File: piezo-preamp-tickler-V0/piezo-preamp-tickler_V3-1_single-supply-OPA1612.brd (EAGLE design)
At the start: 100 x 66 mm, 54 parts, among them IC1 OPA1612, J2 phone/mixer-switch, J3 phone/mixer-switch, Q1 J201, Q1A 2N5486, Q2 MMBFJ201, Q2A 2N5486

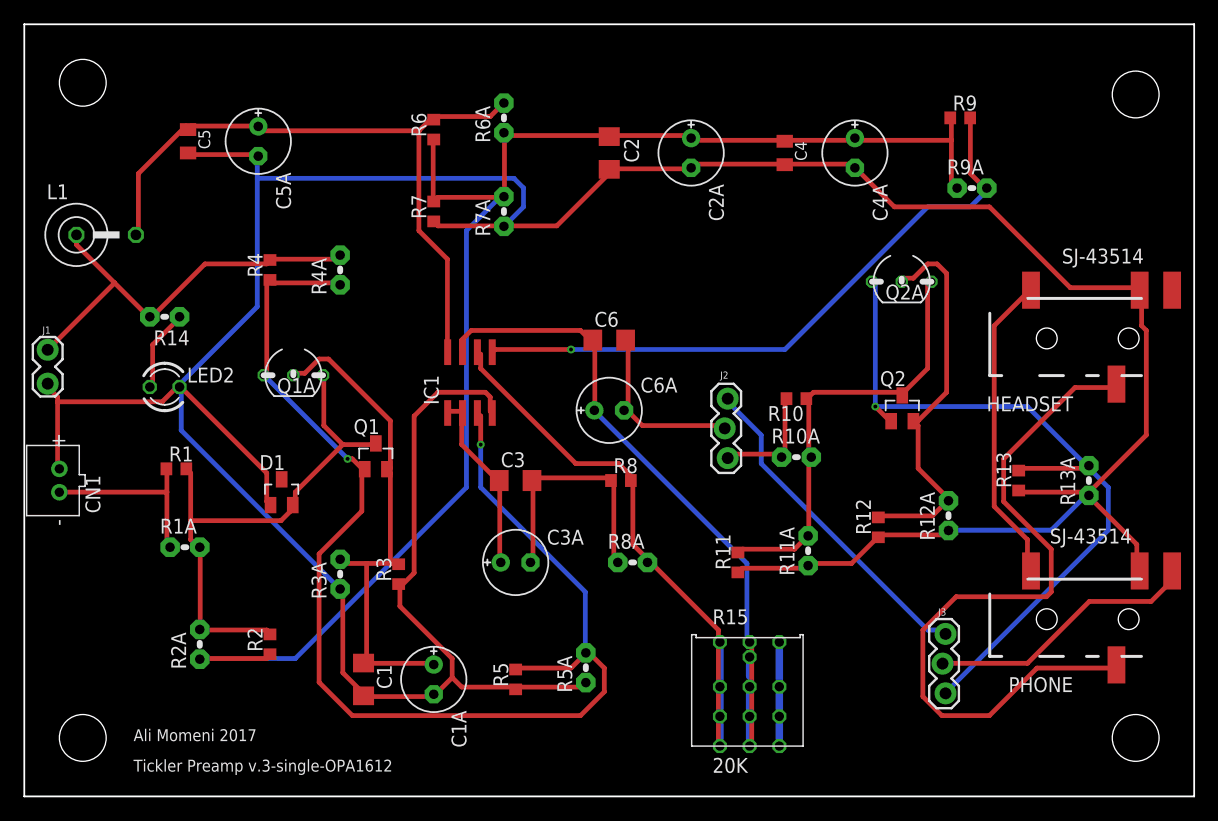
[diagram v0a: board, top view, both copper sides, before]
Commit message: new version so of piezo pickups
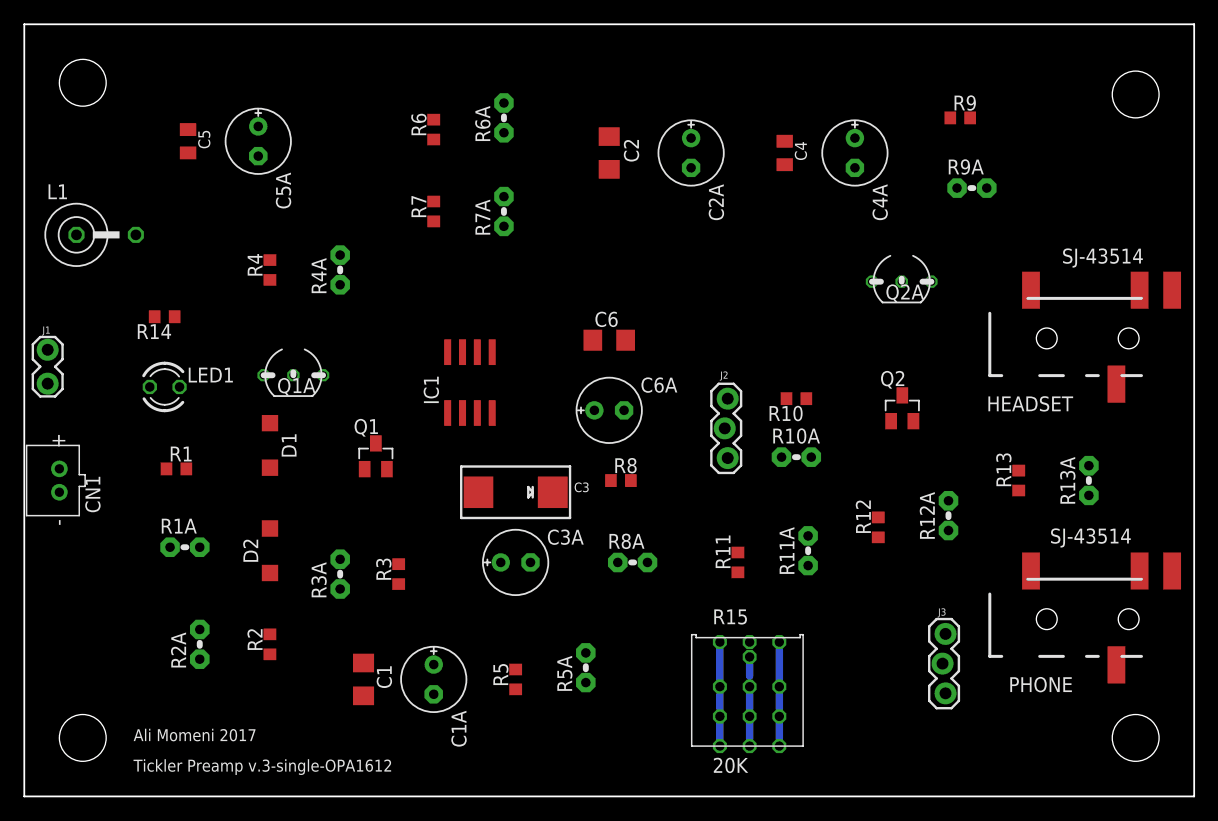
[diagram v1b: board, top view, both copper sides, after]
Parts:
- added D2: 1N4148W, CMU-ArtFab:SOD123
- C3: value 100uF -> mnove; device adafruit:C1206 -> microbuilder:EIA7343-31/D-R
- C4A: value 10uF -> 0.1uF
- D1: value BAT54S -> 1N4148W; device diode:SOT23 -> CMU-ArtFab:SOD123
- R14: device CMU-ArtFab:0204V -> CMU-ArtFab:R0603
- moved D1 4.12 mm to (21.0, 30.0), turned to 270 degrees
- moved C3 1.00 mm to (42.0, 26.0)
- renumbered LED2 to LED1
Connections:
- new net N$4: D1.A, D2.A
- net GATE1: now also D1.C; no longer D1.2
- net GND: now also D2.C; no longer D1.1
- net N$1: now also C3.+; no longer C3.1
- net N$52: now also C3.-; no longer C3.2
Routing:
- net GND: track 309.5 -> 0.00 mm
- net N$35: track 123.3 -> 0.00 mm
- net DRAINE1: track 107.8 -> 0.00 mm, vias 2 -> 0
- net NAME: track 65.1 -> 0.00 mm, vias 1 -> 0
- net N$45: track 62.4 -> 0.00 mm
- net N$32: track 59.9 -> 0.00 mm
- net N$16: track 54.8 -> 0.00 mm, vias 1 -> 0
- net N$31: track 53.8 -> 0.00 mm
- net GATE1: track 46.3 -> 0.00 mm
- net N$22: track 45.0 -> 0.00 mm
- net SOURCE1: track 43.5 -> 0.00 mm
- net GATE2: track 37.9 -> 0.00 mm
- net +12V: track 36.3 -> 0.00 mm
- net SOURCE: track 33.5 -> 0.00 mm
- net N$42: track 28.5 -> 0.00 mm
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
